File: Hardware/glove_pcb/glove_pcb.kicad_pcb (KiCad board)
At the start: 4 copper layers, 124 parts, among them J1 OSTVN02A150, J10 302-R141, J11 61300611121, J12 67997-206HLF, J13 22053061, J2 OSTVN02A150, J3 54-00130, J4 0436500200, J5 0436500200, J6 0436500200, J7 0436500200, J8 0436500200, J9 302-R141, U1 AP63205WU, U10 BZA408B, U11 BZA408B, U12 MCP3008, U13 ATmega328PB-A, U14 MCP3008, U15 MCP3008, U16 BM70BLES1FC2-0B04AA, U17 MCP111T-195I/TT, U18 74LVC1T45GW_125, U19 74LVC1T45GW_125, U2 TCR2EF33_LMCT, U3 DRV8876PWPR, U4 DRV8876PWPR, U5 DRV8876PWPR, U6 DRV8876PWPR, U7 DRV8876PWPR, U8 BZA408B, U9 BZA408B

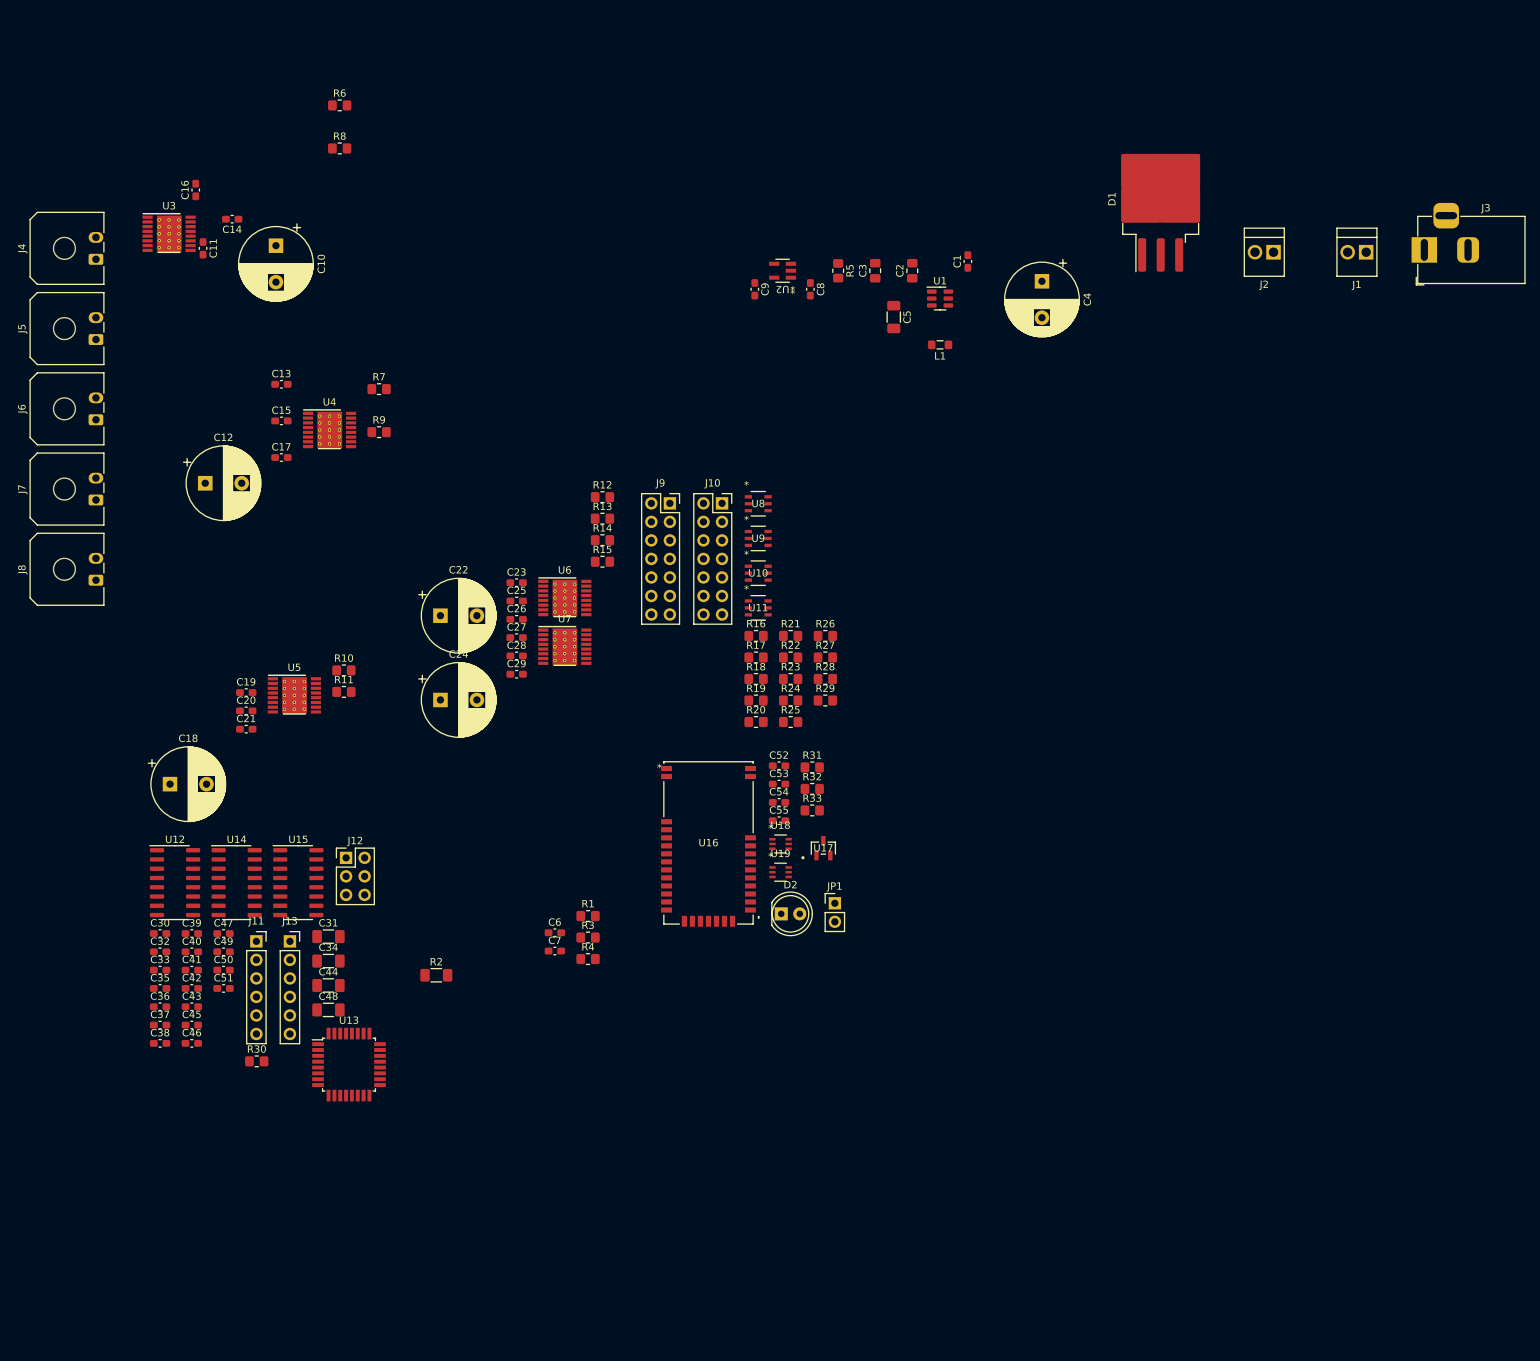
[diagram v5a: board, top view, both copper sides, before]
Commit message: Coarse placement of components
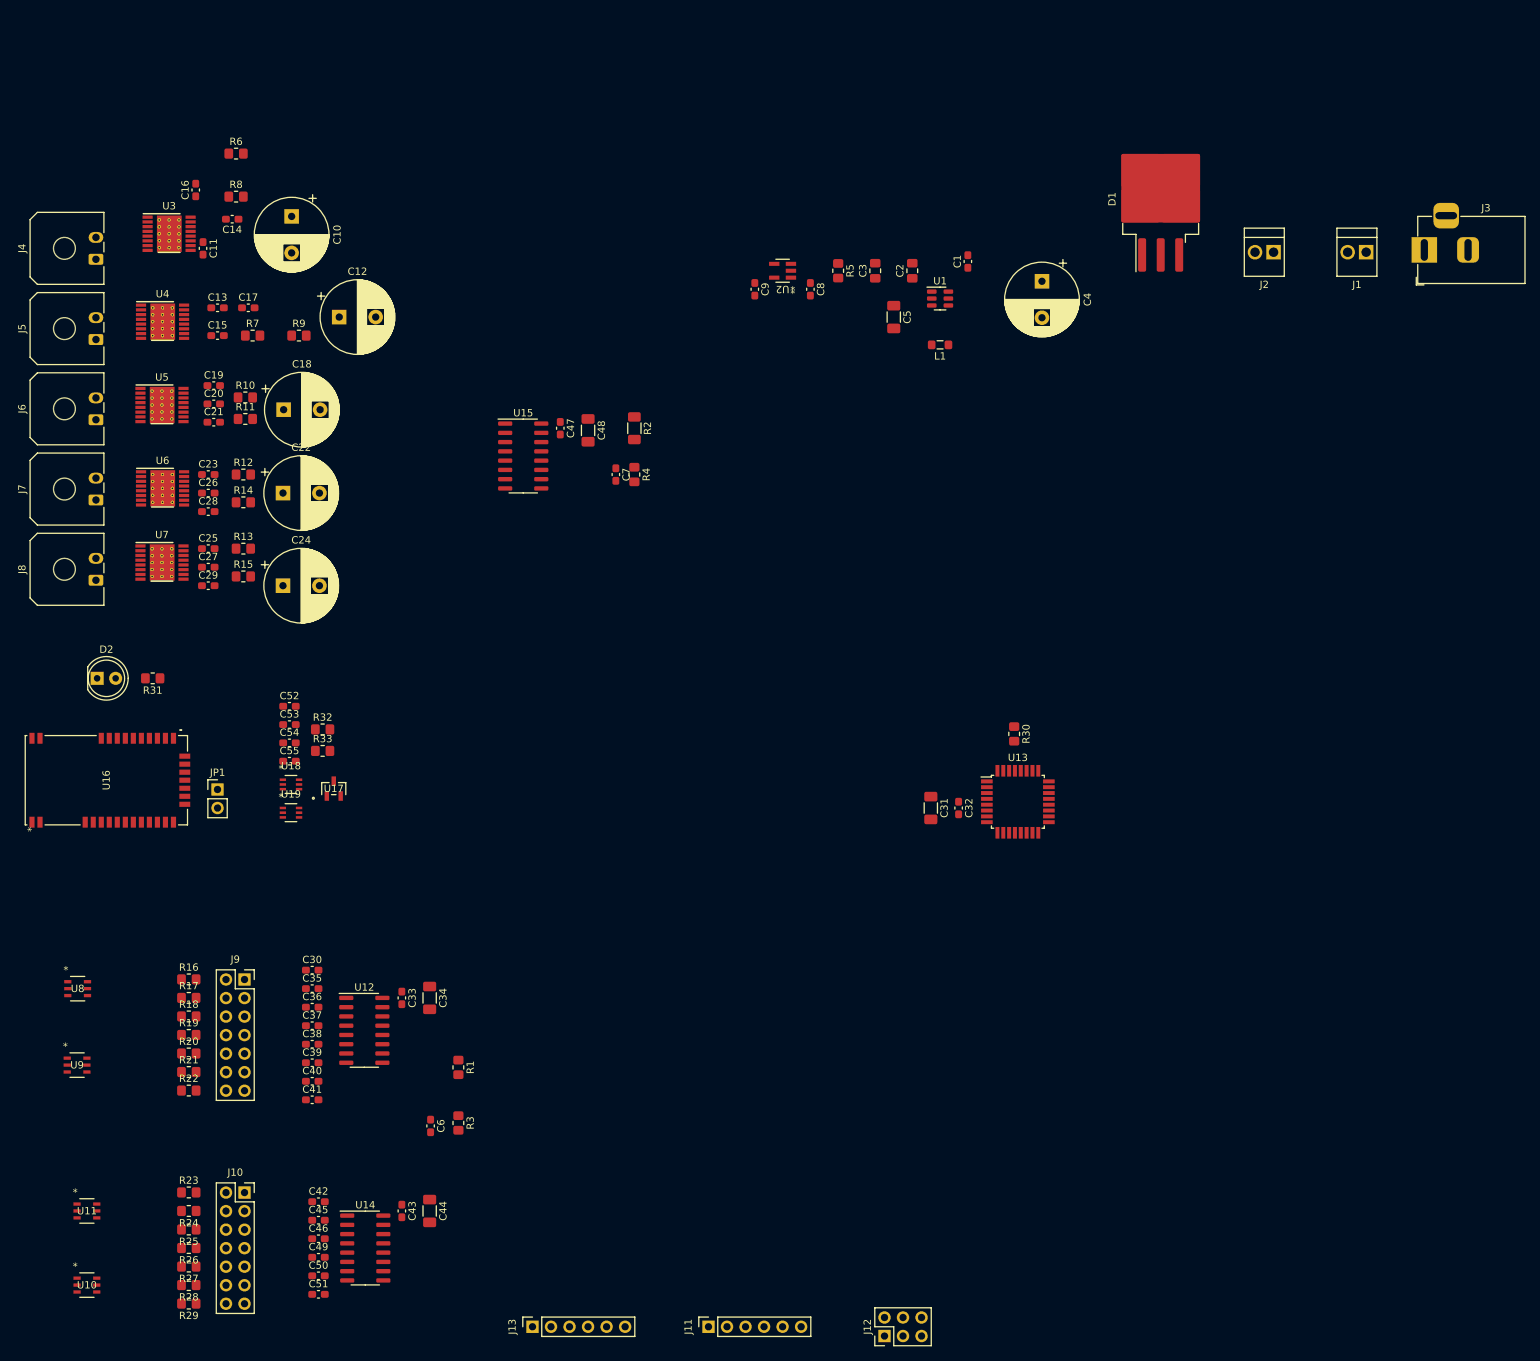
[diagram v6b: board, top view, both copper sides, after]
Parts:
- moved U10 134.2 mm to (29.1, 191.1)
- moved U11 123.7 mm to (29.1, 181.0)
- moved R26 121.1 mm to (43.0, 186.1), turned to 180 degrees
- moved R27 120.8 mm to (43.0, 188.6), turned to 180 degrees
- moved R28 120.5 mm to (43.0, 191.1), turned to 180 degrees
- moved R29 120.2 mm to (43.0, 193.7), turned to 180 degrees
- moved U9 118.0 mm to (27.7, 161.0)
- moved J10 115.0 mm to (50.7, 178.5)
- moved U8 114.6 mm to (27.8, 150.5)
- moved R30 113.1 mm to (156.2, 115.6), turned to -90 degrees
- moved C32 111.2 mm to (148.6, 125.7), turned to -90 degrees
- moved R23 108.5 mm to (43.0, 178.4)
- moved R24 108.2 mm to (43.0, 181.0), turned to 180 degrees
- moved R25 107.9 mm to (43.0, 183.5), turned to 180 degrees
- moved R21 101.9 mm to (43.0, 161.9)
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
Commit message: More tentative placing work
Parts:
- moved C6 130.4 mm to (82.2, 39.0)
- moved R1 130.4 mm to (86.0, 31.0)
- moved R3 130.4 mm to (86.0, 38.6)
- moved J10 129.8 mm to (37.6, 49.3)
- moved U10 129.7 mm to (52.9, 63.7)
- moved U11 129.7 mm to (52.9, 53.5)
- moved C42 129.2 mm to (61.8, 50.6)
- moved C45 129.2 mm to (61.8, 53.1)
- moved C46 129.2 mm to (61.8, 55.6)
- moved C50 129.2 mm to (61.8, 60.7)
- moved C51 129.2 mm to (61.8, 63.3)
- moved U14 129.2 mm to (68.2, 56.9)
- moved C43 129.2 mm to (73.2, 51.8)
- moved C44 129.2 mm to (77.0, 51.8)
- moved C49 129.2 mm to (61.8, 58.2)
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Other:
- board outline added: 120 x 120 mm

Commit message: More placing
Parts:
- moved C47 49.5 mm to (173.9, 102.2)
- moved C48 49.5 mm to (177.7, 102.5)
- moved R2 49.5 mm to (184.1, 102.2)
- moved R4 49.5 mm to (184.1, 108.6)
- moved U15 49.5 mm to (168.8, 106.0)
- moved C7 49.5 mm to (181.5, 108.6)
- moved C31 48.9 mm to (140.5, 77.1)
- moved C32 48.9 mm to (144.3, 77.1)
- moved R30 48.9 mm to (151.9, 66.9)
- moved U13 48.9 mm to (152.4, 76.2)
- moved J12 48.7 mm to (180.3, 81.3), turned to 180 degrees
- moved U8 43.9 mm to (95.3, 23.2)
- moved U9 43.8 mm to (95.2, 35.6)
- moved C41 43.4 mm to (104.1, 45.7)
- moved U11 42.8 mm to (95.3, 47.3)
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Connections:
- U12 pad 8: POT_MIDDLE_3 -> GND
- U14 pad 1: POT_RING_1 -> POT_MIDDLE_3
- U14 pad 2: POT_RING_2 -> POT_RING_1
- U14 pad 3: POT_RING_3 -> POT_RING_2
- U14 pad 4: POT_PINKY_1 -> POT_RING_3
- U14 pad 5: POT_PINKY_2 -> POT_PINKY_1
- U14 pad 6: POT_PINKY_3 -> POT_PINKY_2
- U14 pad 7: GND -> POT_PINKY_3
